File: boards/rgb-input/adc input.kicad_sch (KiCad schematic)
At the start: 4 parts

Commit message: solved the ADC issue and found another minor one
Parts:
- renumbered C3 to C11, R17 to R19
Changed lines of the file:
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@@
   (symbol (lib_id "Device:R_US") (at 156.21 90.17 90) (mirror x) (unit 1)
     (in_bom yes) (on_board yes) (dnp no) (fields_autoplaced)
-    (property "Reference" "R17" (at 156.21 83.82 90)
+    (property "Reference" "R19" (at 156.21 83.82 90)
       (effects (font (size 1.27 1.27)))
     )
@@
     (instances
       (project "rgb-input"
+        (path "/c83c6236-96e9-46ad-9d7a-9e2efa4a7966/f06c9bf0-de4e-49a2-91ec-1c9426377826"
+          (reference "R19") (unit 1)
+        )
+        (path "/c83c6236-96e9-46ad-9d7a-9e2efa4a7966/76149826-8526-4a6c-8e11-6dc0109cc281"
+          (reference "R26") (unit 1)
+        )
+        (path "/c83c6236-96e9-46ad-9d7a-9e2efa4a7966/d24c7443-0875-4d8e-b56e-81b211cd6f3d"
+          (reference "R25") (unit 1)
+        )
+        (path "/c83c6236-96e9-46ad-9d7a-9e2efa4a7966/7fda9512-7a31-4b6e-85db-2478bfe7f375"
+          (reference "R24") (unit 1)
+        )
+        (path "/c83c6236-96e9-46ad-9d7a-9e2efa4a7966/597c781a-3a73-4808-b6ed-8c917478e623"
+          (reference "R23") (unit 1)
+        )
+        (path "/c83c6236-96e9-46ad-9d7a-9e2efa4a7966/1ca70e91-4481-4c96-8c08-39dd142498e5"
+          (reference "R22") (unit 1)
+        )
+        (path "/c83c6236-96e9-46ad-9d7a-9e2efa4a7966/c9e1b2da-9064-45a5-a0a2-ee072f7e1acf"
+          (reference "R21") (unit 1)
+        )
+        (path "/c83c6236-96e9-46ad-9d7a-9e2efa4a7966/120468c6-3bec-414c-9049-57af589f397a"
+          (reference "R20") (unit 1)
+        )
+        (path "/c83c6236-96e9-46ad-9d7a-9e2efa4a7966/ef548cdc-9d5d-4f8e-8f54-0c2e96dbe3f0"
+          (reference "R1") (unit 1)
+        )
         (path "/c83c6236-96e9-46ad-9d7a-9e2efa4a7966/a581b924-afd8-4b56-b69e-790286072066"
           (reference "R17") (unit 1)
         )
-        (path "/c83c6236-96e9-46ad-9d7a-9e2efa4a7966/4f50afed-9381-4977-8e27-209f0f88ad4e"
-          (reference "R3") (unit 1)
+        (path "/c83c6236-96e9-46ad-9d7a-9e2efa4a7966/803edf1a-5825-4947-a8b9-85d3a29697e5"
+          (reference "R15") (unit 1)
+        )
+        (path "/c83c6236-96e9-46ad-9d7a-9e2efa4a7966/802175d5-fb4b-4457-a117-b0f397189ff7"
+          (reference "R13") (unit 1)
+        )
+        (path "/c83c6236-96e9-46ad-9d7a-9e2efa4a7966/5fc618b8-7830-4bbf-bf46-7753631e9b1e"
+          (reference "R11") (unit 1)
+        )
+        (path "/c83c6236-96e9-46ad-9d7a-9e2efa4a7966/145fa34f-e19e-43e2-bb48-aff2e824ef0a"
+          (reference "R9") (unit 1)
+        )
+        (path "/c83c6236-96e9-46ad-9d7a-9e2efa4a7966/6f6f2d8d-82f6-4691-bba7-8caa1bd52e96"
+          (reference "R7") (unit 1)
         )
         (path "/c83c6236-96e9-46ad-9d7a-9e2efa4a7966/4175a172-5c0b-4d6a-88bb-129f5f07b813"
           (reference "R5") (unit 1)
         )
-        (path "/c83c6236-96e9-46ad-9d7a-9e2efa4a7966/6f6f2d8d-82f6-4691-bba7-8caa1bd52e96"
-          (reference "R7") (unit 1)
-        )
-        (path "/c83c6236-96e9-46ad-9d7a-9e2efa4a7966/145fa34f-e19e-43e2-bb48-aff2e824ef0a"
-          (reference "R9") (unit 1)
-        )
-        (path "/c83c6236-96e9-46ad-9d7a-9e2efa4a7966/5fc618b8-7830-4bbf-bf46-7753631e9b1e"
-          (reference "R11") (unit 1)
-        )
-        (path "/c83c6236-96e9-46ad-9d7a-9e2efa4a7966/802175d5-fb4b-4457-a117-b0f397189ff7"
-          (reference "R13") (unit 1)
-        )
-        (path "/c83c6236-96e9-46ad-9d7a-9e2efa4a7966/803edf1a-5825-4947-a8b9-85d3a29697e5"
-          (reference "R15") (unit 1)
-        )
-        (path "/c83c6236-96e9-46ad-9d7a-9e2efa4a7966/f06c9bf0-de4e-49a2-91ec-1c9426377826"
-          (reference "R19") (unit 1)
-        )
-        (path "/c83c6236-96e9-46ad-9d7a-9e2efa4a7966/ef548cdc-9d5d-4f8e-8f54-0c2e96dbe3f0"
-          (reference "R1") (unit 1)
-        )
-        (path "/c83c6236-96e9-46ad-9d7a-9e2efa4a7966/120468c6-3bec-414c-9049-57af589f397a"
-          (reference "R20") (unit 1)
-        )
-        (path "/c83c6236-96e9-46ad-9d7a-9e2efa4a7966/c9e1b2da-9064-45a5-a0a2-ee072f7e1acf"
-          (reference "R21") (unit 1)
-        )
-        (path "/c83c6236-96e9-46ad-9d7a-9e2efa4a7966/1ca70e91-4481-4c96-8c08-39dd142498e5"
-          (reference "R22") (unit 1)
-        )
-        (path "/c83c6236-96e9-46ad-9d7a-9e2efa4a7966/597c781a-3a73-4808-b6ed-8c917478e623"
-          (reference "R23") (unit 1)
-        )
-        (path "/c83c6236-96e9-46ad-9d7a-9e2efa4a7966/7fda9512-7a31-4b6e-85db-2478bfe7f375"
-          (reference "R24") (unit 1)
-        )
-        (path "/c83c6236-96e9-46ad-9d7a-9e2efa4a7966/d24c7443-0875-4d8e-b56e-81b211cd6f3d"
-          (reference "R25") (unit 1)
-        )
-        (path "/c83c6236-96e9-46ad-9d7a-9e2efa4a7966/76149826-8526-4a6c-8e11-6dc0109cc281"
-          (reference "R26") (unit 1)
+        (path "/c83c6236-96e9-46ad-9d7a-9e2efa4a7966/4f50afed-9381-4977-8e27-209f0f88ad4e"
+          (reference "R3") (unit 1)
         )
       )
@@
   (symbol (lib_id "Device:C_Small") (at 162.56 96.52 0) (unit 1)
     (in_bom yes) (on_board yes) (dnp no) (fields_autoplaced)
-    (property "Reference" "C3" (at 165.1 95.2563 0)
+    (property "Reference" "C11" (at 165.1 95.2563 0)
       (effects (font (size 1.27 1.27)) (justify left))
     )
@@
     (instances
       (project "rgb-input"
+        (path "/c83c6236-96e9-46ad-9d7a-9e2efa4a7966/a581b924-afd8-4b56-b69e-790286072066"
+          (reference "C11") (unit 1)
+        )
+        (path "/c83c6236-96e9-46ad-9d7a-9e2efa4a7966/4f50afed-9381-4977-8e27-209f0f88ad4e"
+          (reference "C4") (unit 1)
+        )
+        (path "/c83c6236-96e9-46ad-9d7a-9e2efa4a7966/4175a172-5c0b-4d6a-88bb-129f5f07b813"
+          (reference "C5") (unit 1)
+        )
+        (path "/c83c6236-96e9-46ad-9d7a-9e2efa4a7966/6f6f2d8d-82f6-4691-bba7-8caa1bd52e96"
+          (reference "C6") (unit 1)
+        )
+        (path "/c83c6236-96e9-46ad-9d7a-9e2efa4a7966/145fa34f-e19e-43e2-bb48-aff2e824ef0a"
+          (reference "C7") (unit 1)
+        )
+        (path "/c83c6236-96e9-46ad-9d7a-9e2efa4a7966/5fc618b8-7830-4bbf-bf46-7753631e9b1e"
+          (reference "C8") (unit 1)
+        )
+        (path "/c83c6236-96e9-46ad-9d7a-9e2efa4a7966/802175d5-fb4b-4457-a117-b0f397189ff7"
+          (reference "C9") (unit 1)
+        )
+        (path "/c83c6236-96e9-46ad-9d7a-9e2efa4a7966/803edf1a-5825-4947-a8b9-85d3a29697e5"
+          (reference "C10") (unit 1)
+        )
+        (path "/c83c6236-96e9-46ad-9d7a-9e2efa4a7966/f06c9bf0-de4e-49a2-91ec-1c9426377826"
+          (reference "C12") (unit 1)
+        )
         (path "/c83c6236-96e9-46ad-9d7a-9e2efa4a7966/ef548cdc-9d5d-4f8e-8f54-0c2e96dbe3f0"
           (reference "C3") (unit 1)
+        )
+        (path "/c83c6236-96e9-46ad-9d7a-9e2efa4a7966/120468c6-3bec-414c-9049-57af589f397a"
+          (reference "C13") (unit 1)
+        )
+        (path "/c83c6236-96e9-46ad-9d7a-9e2efa4a7966/c9e1b2da-9064-45a5-a0a2-ee072f7e1acf"
+          (reference "C14") (unit 1)
+        )
+        (path "/c83c6236-96e9-46ad-9d7a-9e2efa4a7966/1ca70e91-4481-4c96-8c08-39dd142498e5"
+          (reference "C15") (unit 1)
+        )
+        (path "/c83c6236-96e9-46ad-9d7a-9e2efa4a7966/597c781a-3a73-4808-b6ed-8c917478e623"
+          (reference "C16") (unit 1)
+        )
+        (path "/c83c6236-96e9-46ad-9d7a-9e2efa4a7966/7fda9512-7a31-4b6e-85db-2478bfe7f375"
+          (reference "C17") (unit 1)
+        )
+        (path "/c83c6236-96e9-46ad-9d7a-9e2efa4a7966/d24c7443-0875-4d8e-b56e-81b211cd6f3d"
+          (reference "C18") (unit 1)
         )
         (path "/c83c6236-96e9-46ad-9d7a-9e2efa4a7966/76149826-8526-4a6c-8e11-6dc0109cc281"
           (reference "C19") (unit 1)
         )
-        (path "/c83c6236-96e9-46ad-9d7a-9e2efa4a7966/d24c7443-0875-4d8e-b56e-81b211cd6f3d"
-          (reference "C18") (unit 1)
-        )
-        (path "/c83c6236-96e9-46ad-9d7a-9e2efa4a7966/7fda9512-7a31-4b6e-85db-2478bfe7f375"
-          (reference "C17") (unit 1)
-        )
-        (path "/c83c6236-96e9-46ad-9d7a-9e2efa4a7966/597c781a-3a73-4808-b6ed-8c917478e623"
-          (reference "C16") (unit 1)
-        )
-        (path "/c83c6236-96e9-46ad-9d7a-9e2efa4a7966/1ca70e91-4481-4c96-8c08-39dd142498e5"
-          (reference "C15") (unit 1)
-        )
-        (path "/c83c6236-96e9-46ad-9d7a-9e2efa4a7966/c9e1b2da-9064-45a5-a0a2-ee072f7e1acf"
-          (reference "C14") (unit 1)
-        )
-        (path "/c83c6236-96e9-46ad-9d7a-9e2efa4a7966/120468c6-3bec-414c-9049-57af589f397a"
-          (reference "C13") (unit 1)
-        )
-        (path "/c83c6236-96e9-46ad-9d7a-9e2efa4a7966/a581b924-afd8-4b56-b69e-790286072066"
-          (reference "C11") (unit 1)
-        )
-        (path "/c83c6236-96e9-46ad-9d7a-9e2efa4a7966/f06c9bf0-de4e-49a2-91ec-1c9426377826"
-          (reference "C12") (unit 1)
-        )
-        (path "/c83c6236-96e9-46ad-9d7a-9e2efa4a7966/803edf1a-5825-4947-a8b9-85d3a29697e5"
-          (reference "C10") (unit 1)
-        )
-        (path "/c83c6236-96e9-46ad-9d7a-9e2efa4a7966/802175d5-fb4b-4457-a117-b0f397189ff7"
-          (reference "C9") (unit 1)
-        )
-        (path "/c83c6236-96e9-46ad-9d7a-9e2efa4a7966/5fc618b8-7830-4bbf-bf46-7753631e9b1e"
-          (reference "C8") (unit 1)
-        )
-        (path "/c83c6236-96e9-46ad-9d7a-9e2efa4a7966/145fa34f-e19e-43e2-bb48-aff2e824ef0a"
-          (reference "C7") (unit 1)
-        )
-        (path "/c83c6236-96e9-46ad-9d7a-9e2efa4a7966/6f6f2d8d-82f6-4691-bba7-8caa1bd52e96"
-          (reference "C6") (unit 1)
-        )
-        (path "/c83c6236-96e9-46ad-9d7a-9e2efa4a7966/4175a172-5c0b-4d6a-88bb-129f5f07b813"
-          (reference "C5") (unit 1)
-        )
-        (path "/c83c6236-96e9-46ad-9d7a-9e2efa4a7966/4f50afed-9381-4977-8e27-209f0f88ad4e"
-          (reference "C4") (unit 1)
-        )
       )

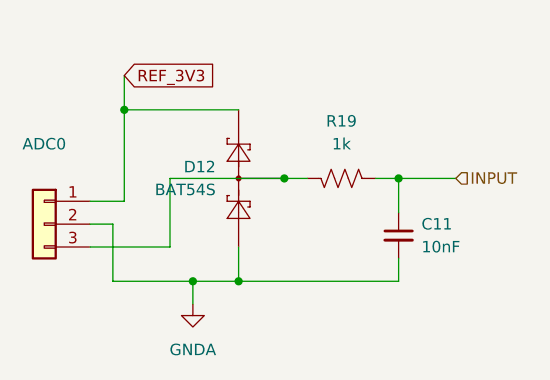
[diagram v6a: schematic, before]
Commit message: first pass on redesign of the rgb input board
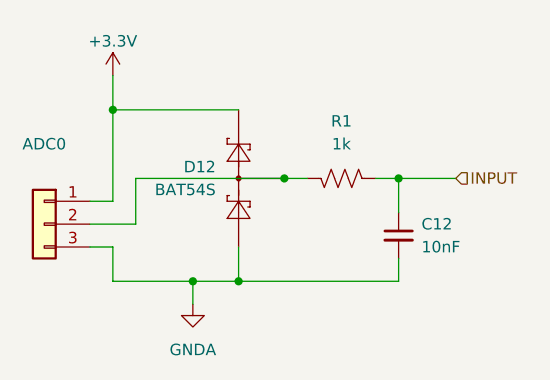
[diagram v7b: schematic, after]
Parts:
- renumbered C11 to C12, R19 to R1
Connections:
- net GNDA: now also ADC0.3 (Pin_3); no longer ADC0.2 (Pin_2)
- net at D12.3 (COM), R1.1: now also ADC0.2 (Pin_2); no longer ADC0.3 (Pin_3)
- net REF_3V3 renamed +3.3V

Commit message: new rgb input board coming along very nicely
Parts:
- renumbered C12 to C11, R1 to R19
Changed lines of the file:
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@@
   (symbol (lib_id "Device:R_US") (at 156.21 90.17 90) (mirror x) (unit 1)
     (in_bom yes) (on_board yes) (dnp no) (fields_autoplaced)
-    (property "Reference" "R1" (at 156.21 83.82 90)
+    (property "Reference" "R19" (at 156.21 83.82 90)
       (effects (font (size 1.27 1.27)))
     )
@@
     (instances
       (project "rgb-input"
-        (path "/c83c6236-96e9-46ad-9d7a-9e2efa4a7966/ef548cdc-9d5d-4f8e-8f54-0c2e96dbe3f0"
-          (reference "R1") (unit 1)
+        (path "/c83c6236-96e9-46ad-9d7a-9e2efa4a7966/f06c9bf0-de4e-49a2-91ec-1c9426377826"
+          (reference "R19") (unit 1)
         )
         (path "/c83c6236-96e9-46ad-9d7a-9e2efa4a7966/4f50afed-9381-4977-8e27-209f0f88ad4e"
@@
           (reference "R15") (unit 1)
         )
-        (path "/c83c6236-96e9-46ad-9d7a-9e2efa4a7966/f06c9bf0-de4e-49a2-91ec-1c9426377826"
-          (reference "R19") (unit 1)
+        (path "/c83c6236-96e9-46ad-9d7a-9e2efa4a7966/ef548cdc-9d5d-4f8e-8f54-0c2e96dbe3f0"
+          (reference "R1") (unit 1)
         )
         (path "/c83c6236-96e9-46ad-9d7a-9e2efa4a7966/120468c6-3bec-414c-9049-57af589f397a"
@@
   (symbol (lib_id "Device:C_Small") (at 162.56 96.52 0) (unit 1)
     (in_bom yes) (on_board yes) (dnp no) (fields_autoplaced)
-    (property "Reference" "C12" (at 165.1 95.2563 0)
+    (property "Reference" "C11" (at 165.1 95.2563 0)
       (effects (font (size 1.27 1.27)) (justify left))
     )
@@
     (instances
       (project "rgb-input"
-        (path "/c83c6236-96e9-46ad-9d7a-9e2efa4a7966/f06c9bf0-de4e-49a2-91ec-1c9426377826"
-          (reference "C12") (unit 1)
-        )
         (path "/c83c6236-96e9-46ad-9d7a-9e2efa4a7966/76149826-8526-4a6c-8e11-6dc0109cc281"
           (reference "C19") (unit 1)
@@
           (reference "C13") (unit 1)
         )
+        (path "/c83c6236-96e9-46ad-9d7a-9e2efa4a7966/f06c9bf0-de4e-49a2-91ec-1c9426377826"
+          (reference "C12") (unit 1)
+        )
         (path "/c83c6236-96e9-46ad-9d7a-9e2efa4a7966/ef548cdc-9d5d-4f8e-8f54-0c2e96dbe3f0"
